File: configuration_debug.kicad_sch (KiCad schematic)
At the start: 8 parts, among them J3 A2541WV-2x4P, SW1 SW_DIP_x04, U4 HT7533-1_C14289

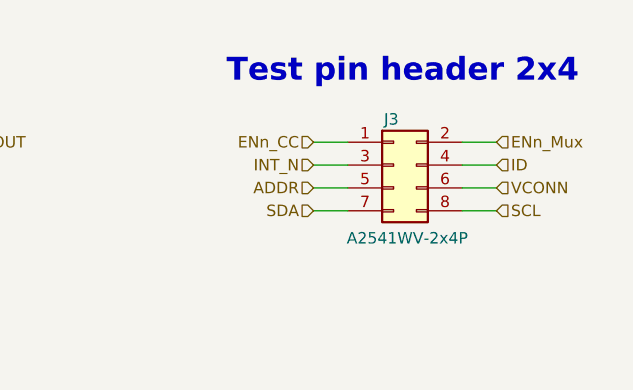
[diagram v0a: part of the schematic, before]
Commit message: Routing Complete (DRC Checker Errors needs fixing)
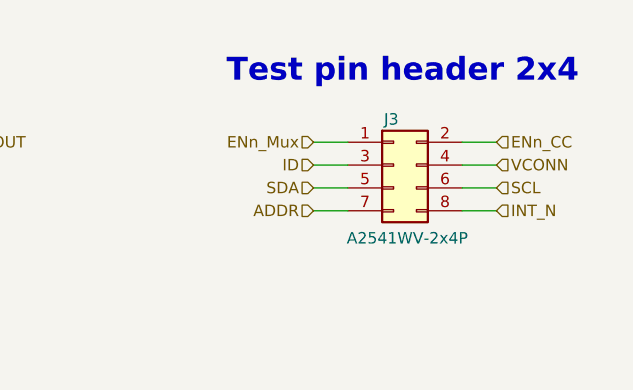
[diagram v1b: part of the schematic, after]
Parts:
- C7, C8: footprint Capacitor_SMD:C_0603_1608Metric -> Capacitor_SMD:C_0402_1005Metric
- R3, R4, R5: footprint Resistor_SMD:R_0603_1608Metric -> Resistor_SMD:R_0402_1005Metric
- U4: footprint footprint:SOT-89-3_L4.5-W2.5-P1.50-LS4.2-BR -> Interface_USB:SOT-89-3_L4.5-W2.5-P1.50-LS4.2-BR
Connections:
- net ADDR: now also J3.7 (Pin_7); no longer J3.5 (Pin_5)
- net ENn_CC: now also J3.2 (Pin_2); no longer J3.1 (Pin_1)
- net ENn_Mux: now also J3.1 (Pin_1); no longer J3.2 (Pin_2)
- net ID: now also J3.3 (Pin_3); no longer J3.4 (Pin_4)
- net INT_N: now also J3.8 (Pin_8); no longer J3.3 (Pin_3)
- net SCL: now also J3.6 (Pin_6); no longer J3.8 (Pin_8)
- net SDA: now also J3.5 (Pin_5); no longer J3.7 (Pin_7)
- net VCONN: now also J3.4 (Pin_4); no longer J3.6 (Pin_6)
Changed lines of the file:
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@@
 	(hierarchical_label "ENn_CC"
 		(shape input)
-		(at 212.09 95.25 180)
+		(at 232.41 95.25 0)
 		(effects
 			(font
 				(size 1.27 1.27)
 			)
+			(justify left)
+		)
+	)
+	(hierarchical_label "INT_N"
+		(shape input)
+		(at 232.41 102.87 0)
+		(effects
+			(font
+				(size 1.27 1.27)
+			)
+			(justify left)
+		)
+	)
+	(hierarchical_label "ADDR"
+		(shape input)
+		(at 212.09 102.87 180)
+		(effects
+			(font
+				(size 1.27 1.27)
+			)
 			(justify right)
 		)
 	)
 	(hierarchical_label "ID"
+		(shape input)
+		(at 212.09 97.79 180)
+		(effects
+			(font
+				(size 1.27 1.27)
+			)
+			(justify right)
+		)
+	)
+	(hierarchical_label "VCONN"
 		(shape input)
 		(at 232.41 97.79 0)
@@
 	(hierarchical_label "SDA"
 		(shape input)
-		(at 212.09 102.87 180)
-		(effects
-			(font
-				(size 1.27 1.27)
-			)
-			(justify right)
-		)
-	)
-	(hierarchical_label "ADDR"
-		(shape input)
 		(at 212.09 100.33 180)
 		(effects
@@
 	(hierarchical_label "SCL"
 		(shape input)
-		(at 232.41 102.87 0)
-		(effects
-			(font
-				(size 1.27 1.27)
-			)
-			(justify left)
-		)
-	)
-	(hierarchical_label "INT_N"
-		(shape input)
-		(at 212.09 97.79 180)
-		(effects
-			(font
-				(size 1.27 1.27)
-			)
-			(justify right)
-		)
-	)
-	(hierarchical_label "ENn_Mux"
-		(shape input)
-		(at 232.41 95.25 0)
+		(at 232.41 100.33 0)
 		(effects
 			(font
@@
 		)
 	)
-	(hierarchical_label "VCONN"
+	(hierarchical_label "ENn_Mux"
 		(shape input)
-		(at 232.41 100.33 0)
+		(at 212.09 95.25 180)
 		(effects
 			(font
 				(size 1.27 1.27)
 			)
-			(justify left)
+			(justify right)
 		)
 	)
@@
 			)
 		)
-		(property "Footprint" "Capacitor_SMD:C_0603_1608Metric"
+		(property "Footprint" "Capacitor_SMD:C_0402_1005Metric"
 			(at 132.08 102.87 0)
 			(hide yes)
@@
 			)
 		)
-		(property "Footprint" "Resistor_SMD:R_0603_1608Metric"
+		(property "Footprint" "Resistor_SMD:R_0402_1005Metric"
 			(at 49.53 96.52 0)
 			(hide yes)
@@
 			)
 		)
-		(property "Footprint" "Resistor_SMD:R_0603_1608Metric"
+		(property "Footprint" "Resistor_SMD:R_0402_1005Metric"
 			(at 80.01 99.06 0)
 			(hide yes)
@@
 			)
 		)
-		(property "Footprint" "Resistor_SMD:R_0603_1608Metric"
+		(property "Footprint" "Resistor_SMD:R_0402_1005Metric"
 			(at 80.01 101.6 0)
 			(hide yes)
@@
 			)
 		)
-		(property "Footprint" "footprint:SOT-89-3_L4.5-W2.5-P1.50-LS4.2-BR"
+		(property "Footprint" "Interface_USB:SOT-89-3_L4.5-W2.5-P1.50-LS4.2-BR"
 			(at 154.686 115.57 0)
 			(hide yes)
@@
 			)
 		)
-		(property "Footprint" "Capacitor_SMD:C_0603_1608Metric"
+		(property "Footprint" "Capacitor_SMD:C_0402_1005Metric"
 			(at 167.64 102.87 0)
 			(hide yes)

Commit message: DRC Errors Fixed, BOM Cleaned up and Generated, Gerber Generated
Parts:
- C7, C8: LCSC (none) -> C7472949; Store Page (none) -> https://www.lcsc.com/product-detail/C7472949.html; Unit Price (none) -> 0.0099
- J3: LCSC (none) -> C225519; Store Page (none) -> https://item.szlcsc.com/225802.html; Unit Price (none) -> 0.1535
- R3: LCSC (none) -> C242161; Store Page (none) -> https://item.szlcsc.com/241007.html; Unit Price (none) -> 0.0051
- R4: footprint Resistor_SMD:R_0402_1005Metric -> Resistor_SMD:R_0805_2012Metric; LCSC (none) -> C316218; Store Page (none) -> https://www.lcsc.com/product-detail/C316218.html; Unit Price (none) -> 0.0420
- R5: LCSC (none) -> C4326584; Store Page (none) -> https://www.lcsc.com/product-detail/C4326584.html; Unit Price (none) -> 0.0570
- SW1: LCSC (none) -> C3293144; Store Page (none) -> https://item.szlcsc.com/3856579.html; Unit Price (none) -> 0.5227
- U4: Store Page (none) -> https://item.szlcsc.com/421845.html; Unit Price (none) -> 0.1202
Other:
- note added: "Switches Configuration Notes: 1 nor 2 closed: NC - DRP 1 closed: Low - UFP 2 closed: High - DFP 3 nor 4 closed: Default - 900mA 3 closed: Medium - 1.5A 4 closed: High - 3A"
- company: (none) -> UWaterloo Reality Labs
- title: (none) -> USB-3.0 Power Management and Configuration Modules
